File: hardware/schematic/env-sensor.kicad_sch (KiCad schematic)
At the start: 58 parts, among them J1 USB-C 16P, J2 JST-PH 2P, SW1 SW_PROV, U1 ESP32-C6-MINI-1-N4, U2 SHT45-AD1F, U3 TPS62840DLC, U4 BQ24074RGTR, U5 USBLC6-2SC6

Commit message: chore(hw): regenerate both boards and previews after review fixes
Emit shared electrical corrections, validated routing and strengthened rules. Development allowances: A54/B58 unrouted and A6/B10 warnings per e584c6a; zero errors and parity differences. Preserve native KiCad SVG formatting. These are draft boards.
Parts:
- R6: value 52k3 1% -> 267k 1%
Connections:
- net +3V0: now also R2.1
- net GND: no longer D1.2 (A), U4.14 (TMR)
- net LED_A: now also D1.2 (A), R2.2; no longer D1.1 (K), R2.1
- net LED_N: now also D1.1 (K); no longer R2.2
- net VSYS: no longer R5.2, U3.4 (EN)
- new net EN_REG: R5.2, U3.4 (EN)
- no-connect marks 19 -> 20
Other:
- note added: "03 System regulator 3.30 V baseline"
- note removed: "03 System regulator 3.00 V"
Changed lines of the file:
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@@
 		)
 	)
-	(text "03  System regulator  3.00 V"
+	(text "03  System regulator  3.30 V baseline"
 		(exclude_from_sim yes)
 		(at 533.4 33.02 0)
@@
 			)
 		)
-		(property "Value" "52k3 1%"
+		(property "Value" "267k 1%"
 			(at 673.1 151.13 0)
 			(effects
@@
 	(wire
 		(pts
-			(xy 304.8 219.71) (xy 300.99 219.71)
-		)
-		(stroke
-			(width 0)
-			(type default)
-		)
-	)
-	(wire
-		(pts
 			(xy 304.8 212.09) (xy 300.99 212.09)
 		)
@@
 		)
 	)
-	(global_label "LED_A"
+	(global_label "LED_N"
 		(shape bidirectional)
 		(at 679.45 226.06 180.0)
@@
 		)
 	)
-	(global_label "GND"
+	(global_label "LED_A"
 		(shape bidirectional)
 		(at 694.69 226.06 0.0)
@@
 		)
 	)
-	(global_label "LED_A"
+	(global_label "+3V0"
 		(shape bidirectional)
 		(at 558.8 255.27 90.0)
@@
 		)
 	)
-	(global_label "LED_N"
+	(global_label "LED_A"
 		(shape bidirectional)
 		(at 558.8 270.51 270.0)
@@
 		)
 	)
-	(global_label "VSYS"
+	(global_label "EN_REG"
 		(shape bidirectional)
 		(at 554.99 87.63 180.0)
@@
 		)
 	)
-	(global_label "VSYS"
+	(global_label "EN_REG"
 		(shape bidirectional)
 		(at 615.95 146.05 270.0)
@@
 		)
 	)
-	(global_label "GND"
-		(shape bidirectional)
-		(at 300.99 219.71 180.0)
-		(fields_autoplaced yes)
-		(effects
-			(font
-				(size 1.27 1.27)
-			)
-			(justify right)
-		)
-	)
 	(global_label "ITERM"
 		(shape bidirectional)
@@
 	)
 	(no_connect
+		(at 304.8 219.71)
+	)
+	(no_connect

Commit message: chore(hw): regenerate both variants for power architecture
Regenerate the shared schematic, both PCB layouts, symbol library, BOM, netlist, enclosure parameters, cost reports and floorplan previews from the updated electrical platform.

Record the reviewed KiCad 10 development budget: zero errors and parity differences, with 59 unrouted items on A and 60 on B. These artifacts remain non-release drafts.
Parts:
- added Q1: 2N7002, sensorly:SOT-23, symbol sensorly:Q_NMOS_GSD
- added R18: 47k 1%, sensorly:R_0402_1005Metric, symbol sensorly:R
- J2: value JST-PH 2P -> Molex PicoBlade 3P; footprint sensorly:JST_PH_S2B-PH-SM4-TB_1x02-1MP_P2.00mm_Horizontal -> sensorly:Molex_PicoBlade_53261-0371_1x03-1MP_P1.25mm_Horizontal; symbol sensorly:Conn_01x02_MountingPin -> sensorly:Conn_01x03_MountingPin
- R11: value 3k09 1% -> 8k00 1%
- R13: value 3k57 1% -> 4k42 1%
- R7: value 10k 1% -> 100k 1%
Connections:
- net EN2 is gone; now on net GND: R8.2, U4.5 (EN2)
- net GND: now also J2.1 (Pin_1), Q1.2 (S); no longer J2.2 (Pin_2), J2.MP (MountPin), U4.4 (~{CE}), U4.6 (EN1)
- net VBAT: now also J2.3 (Pin_3); no longer J2.1 (Pin_1)
- net VBUS: now also R18.2; no longer R8.1
- net CHARGE_ENABLE: now reaches U1.24 (IO18)
- net CHARGE_ENABLE: now also R7.1, Q1.1 (G)
- net USB_ISEL: now reaches U1.27 (IO21)
- net USB_ISEL: now also R8.1, U4.6 (EN1)
- net PACK_TS: now reaches U1.6 (IO3)
- net PACK_TS: now also J2.2 (Pin_2), U4.1 (TS)
- removed net TS: R7.1, U4.1 (TS)
- new net CHARGE_EN_N: Q1.3 (D), R18.1, U4.4 (~{CE})
- no-connect marks 20 -> 18
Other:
- moved on the sheet: C10, C11, C12, C9, R10, R11, R12, R13, R7, R8, R9

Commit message: chore(hw): regenerate the controlled prototype checkpoint
Regenerate shared schematic/BOM/netlist, both PCB projects/rules and floorplan SVGs from the electrical, library and routing corrections in 3c343e2, 135b78b, d863f52, 7802bdf, 0852837 and 7206b19. Preserve R21 DNP and the common A/B electrical platform.

Fresh KiCad 10.0.6: zero ERC violations; both boards have zero DRC errors, warnings and schematic parity differences, with no ignored checks. Development routing exception: A59/B52 unconnected items remain, explicitly recorded in the budget; all old warning allowances are removed. Prototype and product manufacturing gates still require complete routing and real qualification evidence. Full committed-source pipeline follows before push.
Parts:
- added R19, R20: 100k 1%, sensorly:R_0402_1005Metric, symbol sensorly:R
- added R21: 0R, sensorly:R_0402_1005Metric, symbol sensorly:R
- added R22: 10k 1%, sensorly:R_0402_1005Metric, symbol sensorly:R
- C1: value 22uF/6.3V X5R -> 10uF/16V X5R
- C10, C11: value 10uF/6.3V X5R -> 10uF/16V X5R
- C3, C4: value 1uF/16V X7R -> 1uF/16V X5R
- C8: value 10uF/6.3V X5R -> 10uF/16V X5R; footprint sensorly:C_0603_1608Metric -> sensorly:C_0805_2012Metric
- D1: footprint sensorly:LED_0603_1608Metric -> sensorly:Kingbright_KP1608SGC; symbol sensorly:LED -> sensorly:KP1608SGC
- L1: footprint sensorly:L_Murata_DFE201610P -> sensorly:L_Murata_DFE201612E
- Q1: footprint sensorly:SOT-23 -> sensorly:Onsemi_CASE318_SOT23
- R11: value 8k00 1% -> 8k06 1%
- TP10: value USB_DP -> USB_D_P
- TP11: value USB_DM -> USB_D_N
- TP7: value BTN_PROV -> BOOT_N
- U4: footprint sensorly:VQFN-16-1EP_3x3mm_P0.5mm_EP1.6x1.6mm -> sensorly:TI_RGT0016B_VQFN16_3x3mm
- U5: footprint sensorly:SOT-23-6 -> sensorly:ST_USBLC6_SOT23_6
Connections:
- net +3V0: now also R8.2, R19.2, R20.2, R22.2
- net BTN_PROV: now also U1.13 (IO1), R19.1; no longer TP7.1, U1.23 (IO9)
- net GND: no longer R8.2, U4.5 (EN2)
- net LED_A: now also D1.1 (A); no longer D1.2 (A)
- net LED_N: now also D1.2 (K); no longer D1.1 (K)
- net PACK_TS: now also R21.1; no longer U1.6 (IO3)
- net USB_EN2: now reaches U1.19 (IO14)
- net USB_EN2: now also U4.5 (EN2), R20.1
- net BOOT_MODE_H: now reaches U1.22 (IO8)
- net BOOT_MODE_H: now also R22.1
- net USB_DM renamed USB_D_N
- net USB_DP renamed USB_D_P
- new net BOOT_N: TP7.1, U1.23 (IO9)
- new net PACK_TS_SENSE: R21.2, U1.6 (IO3)
- no-connect marks 18 -> 15
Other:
- moved on the sheet: C10, C11, C12, C9, D1, R2

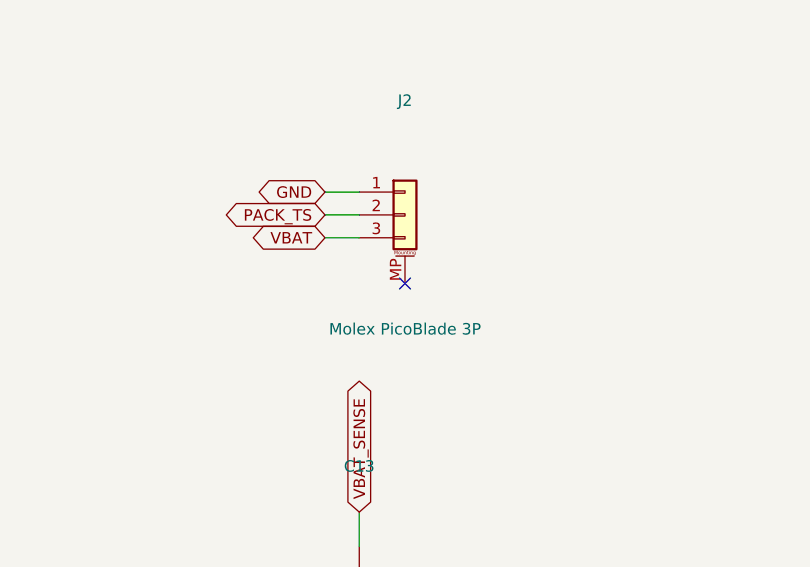
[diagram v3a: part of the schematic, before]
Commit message: build(sch): regenerate connector mounting-ground connectivity
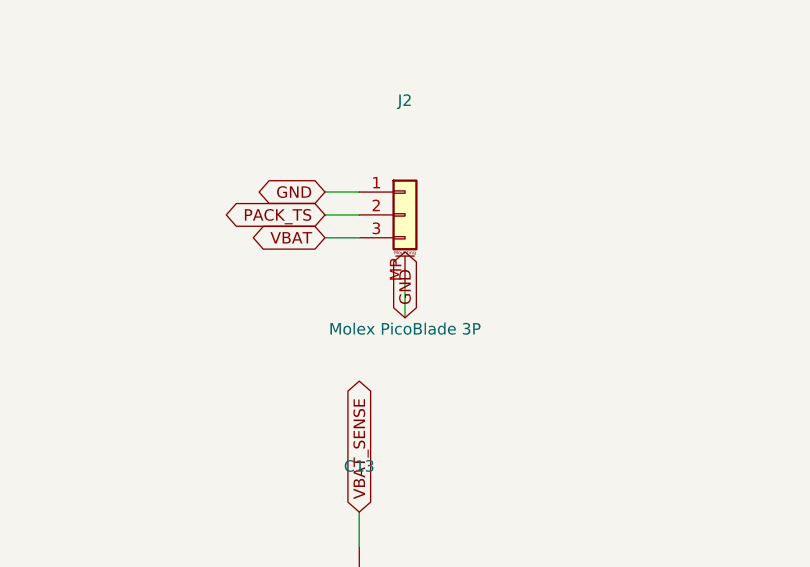
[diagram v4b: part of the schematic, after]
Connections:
- net GND: now also J2.MP (MountPin)
- no-connect marks 15 -> 14
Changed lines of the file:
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@@
+	(wire
+		(pts
+			(xy 309.88 443.23) (xy 309.88 447.04)
+		)
+		(stroke
+			(width 0)
+			(type default)
+		)
+	)
 	(wire
 		(pts
@@
 			)
 			(justify right)
+		)
+	)
+	(global_label "GND"
+		(shape bidirectional)
+		(at 309.88 447.04 270.0)
+		(fields_autoplaced yes)
+		(effects
+			(font
+				(size 1.27 1.27)
+			)
+			(justify left)
 		)
 	)
@@
 		(at 81.28 280.67)
 	)
-	(no_connect
-		(at 309.88 443.23)
-	)
 	(sheet_instances
